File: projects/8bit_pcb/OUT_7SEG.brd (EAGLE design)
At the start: 100 x 80 mm, 26 parts, among them IC4 74LS139N, IC5 NE555N

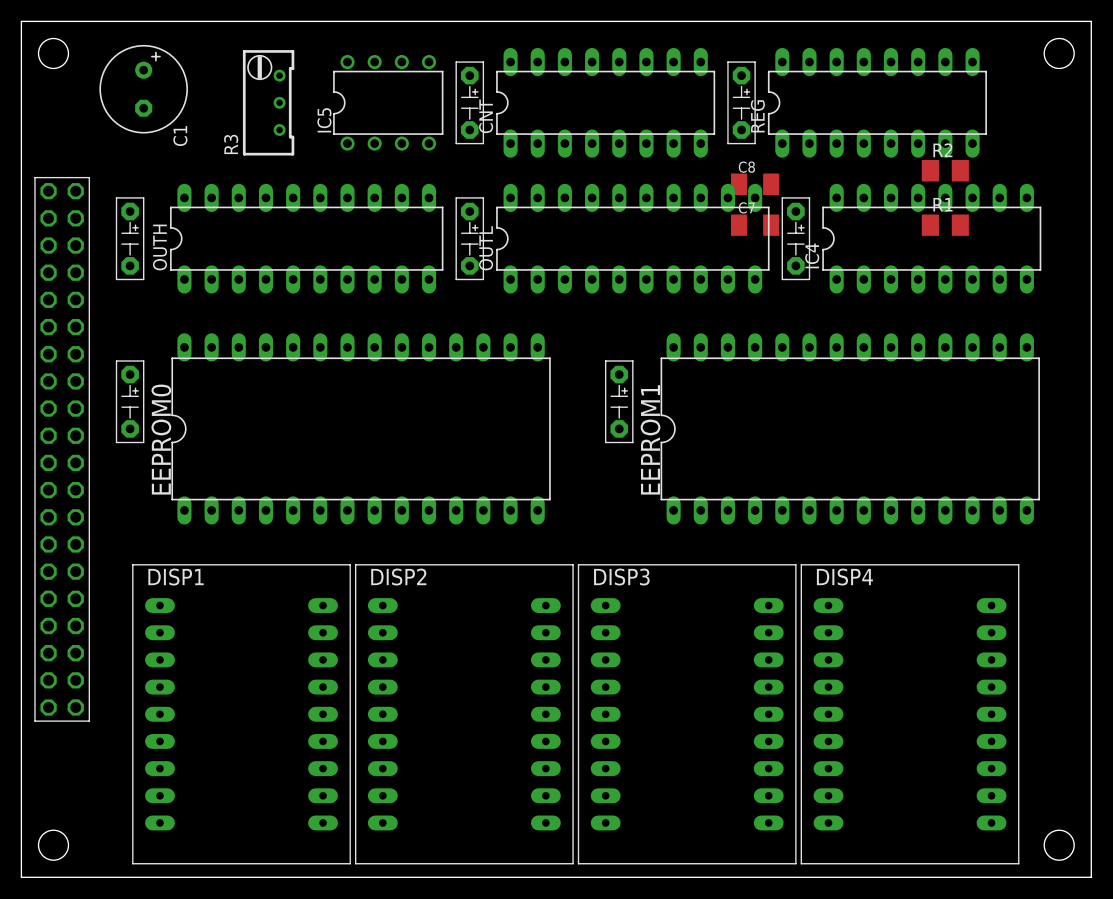
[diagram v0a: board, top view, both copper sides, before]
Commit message: RAM, Disp16Seg, Decoder
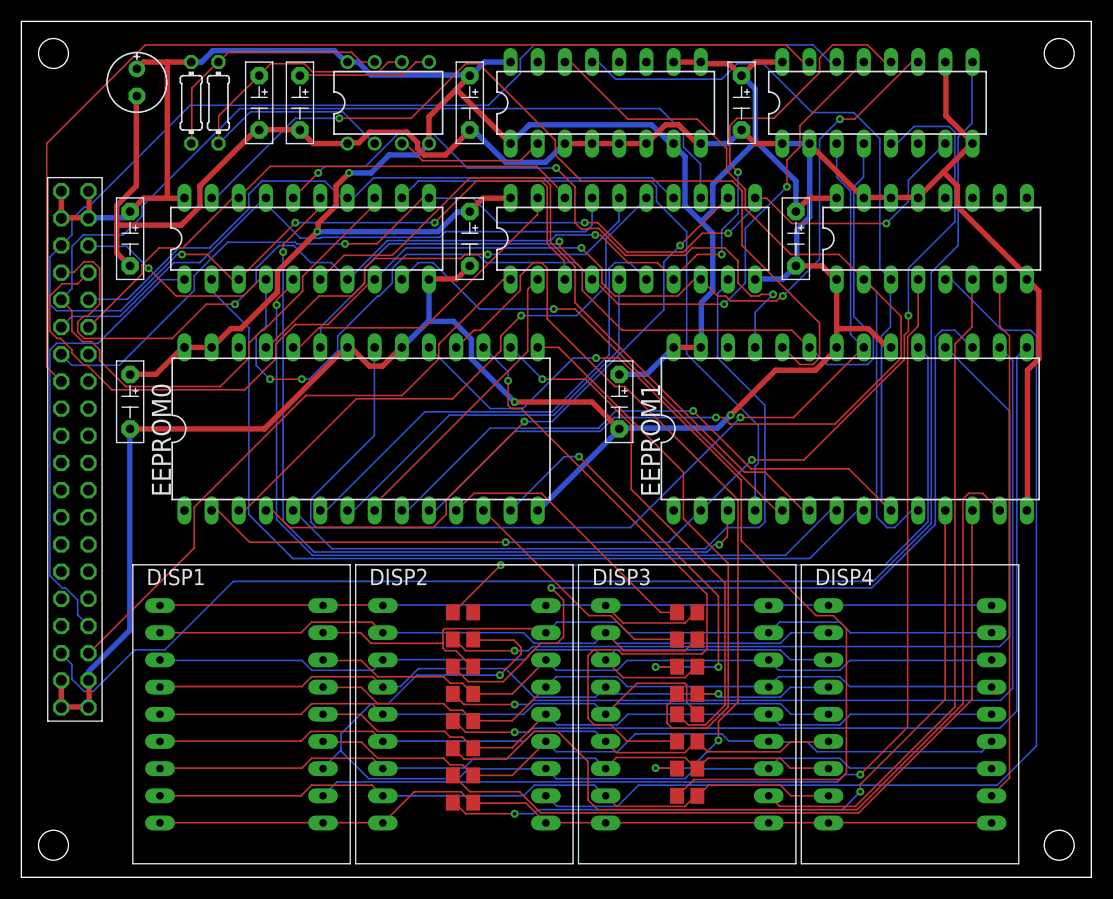
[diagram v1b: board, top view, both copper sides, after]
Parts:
- removed C1: (no value), rcl:E3,5-8
- removed C7: (no value), rcl:C1206K
- added R10, R11, R12, R13, R14, R15, R16, R17, R41, R6, R7, R8, R9: 330, rcl:R0805
- added R4: 1k, rcl:0204/7
- added R5: 100k, rcl:0204/7
- added U$10, U$9: CAP, IsaacAlonso:CAP
- C8: value (none) -> 10n; device rcl:C1206K -> rcl:E2,5-6E
- R1, R2: value (none) -> 330; device rcl:M1206 -> rcl:R0805
- R3: value (none) -> 330; device rcl:RTRIM64W -> rcl:R0805
- moved R2 70.3 mm to (41.3, 12.1)
- moved R1 68.4 mm to (41.3, 9.53)
- moved R3 60.6 mm to (41.3, 14.6)
- moved C8 58.6 mm to (10.8, 74.3), turned to 270 degrees
- moved U$1 1.19 mm to (5.00, 40.0)
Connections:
- removed net N$33: IC5.7, R1.2, R2.1
- removed net N$34: C8.1, IC5.5
- new net ICLK: U$1.P33
- new net N$1: IC5.7, R4.1, R5.2
- new net N$10: EEPROM1.19, R9.1
- new net N$11: EEPROM0.11, R10.1
- new net N$12: EEPROM0.12, R11.1
- new net N$13: EEPROM0.13, R12.1
- new net N$14: EEPROM0.15, R13.1
- new net N$15: EEPROM0.16, R14.1
- new net N$16: EEPROM0.17, R16.1
- new net N$17: EEPROM0.18, R15.1
- new net N$18: EEPROM0.19, R17.1
- new net N$2: IC5.5, U$9.P+
- new net N$3: EEPROM1.11, R41.1
- new net N$4: EEPROM1.12, R1.1
- new net N$6: EEPROM1.15, R3.1
- new net N$7: EEPROM1.16, R6.1
- new net N$8: EEPROM1.17, R7.1
- new net N$9: EEPROM1.18, R8.1
- net !WR_AUX: now also U$1.P17
- net !WR_OUTH: now also U$1.P23
- net !WR_OUTL: now also U$1.P22
- net BUS0: now also U$1.P2
- net BUS1: now also U$1.P37
- net BUS2: now also U$1.P3
- net BUS3: now also U$1.P36
- net BUS4: now also U$1.P4
- net BUS5: now also U$1.P35
- net BUS6: now also U$1.P5
- net BUS7: now also U$1.P34
- net CLK: now also U$1.P6
- net CLK2: now also CNT.2
- net GND: now also C8.-, IC4.13, IC4.14, IC4.15, U$1.P20, U$1.P21, U$10.P-, U$9.P-; no longer C1.-, C7.2, C8.2
- net N$36: now also R5.1, U$10.P+; no longer C7.1, R1.1
- net N$5: now also EEPROM1.13, R2.1; no longer U$1.P20, U$1.P21
- net OUT_0: now also R10.2; no longer EEPROM0.11
- net OUT_1: now also R11.2; no longer EEPROM0.12
- net OUT_10: now also R2.2; no longer EEPROM1.13
- net OUT_11: now also R3.2; no longer EEPROM1.15
- net OUT_12: now also R6.2; no longer EEPROM1.16
- net OUT_13: now also R7.2; no longer EEPROM1.17
- net OUT_14: now also R8.2; no longer EEPROM1.18
- net OUT_15: now also R9.2; no longer EEPROM1.19
- net OUT_2: now also R12.2; no longer EEPROM0.13
- net OUT_3: now also R13.2; no longer EEPROM0.15
- net OUT_4: now also R14.2; no longer EEPROM0.16
- net OUT_5: now also R16.2; no longer EEPROM0.17
- net OUT_6: now also R15.2; no longer EEPROM0.18
- net OUT_7: now also R17.2; no longer EEPROM0.19
- net OUT_8: now also R41.2; no longer EEPROM1.11
- net OUT_9: now also R1.2; no longer EEPROM1.12
- net RST: now also U$1.P7
- net VCC: now also C8.+, CNT.1, CNT.10, CNT.7, CNT.9, R4.2; no longer C1.+, R2.2
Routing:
- net GND: track 0.00 -> 323.4 mm, vias 0 -> 2
- net VCC: track 0.00 -> 227.7 mm, vias 0 -> 2
- net BUS0: track 0.00 -> 151.7 mm, vias 0 -> 3
- net !WR_AUX: track 0.00 -> 134.9 mm
- net CNT0: track 0.00 -> 125.6 mm, vias 0 -> 1
- net CNT1: track 0.00 -> 120.4 mm, vias 0 -> 1
- net BUS4: track 0.00 -> 119.8 mm
- net BUS3: track 0.00 -> 117.6 mm, vias 0 -> 3
- net BUS2: track 0.00 -> 114.6 mm, vias 0 -> 4
- net BUS1: track 0.00 -> 108.3 mm, vias 0 -> 5
- net AUX_2: track 0.00 -> 103.1 mm, vias 0 -> 3
- net CLK: track 0.00 -> 100.4 mm, vias 0 -> 4
- net !EN0: track 0.00 -> 99.6 mm, vias 0 -> 1
- net RST: track 0.00 -> 98.6 mm
- net AUX_0: track 0.00 -> 97.8 mm, vias 0 -> 1
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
